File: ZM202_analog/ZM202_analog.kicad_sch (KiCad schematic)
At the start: 8 parts, among them U1 LM324, U13 LM393B

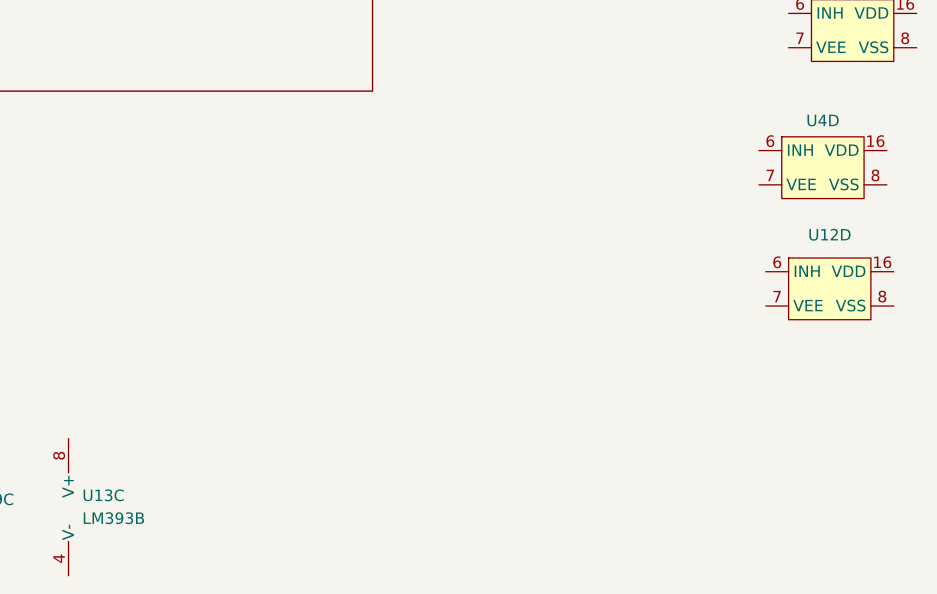
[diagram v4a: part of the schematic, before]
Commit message: Added PLL-circuit and added labels.
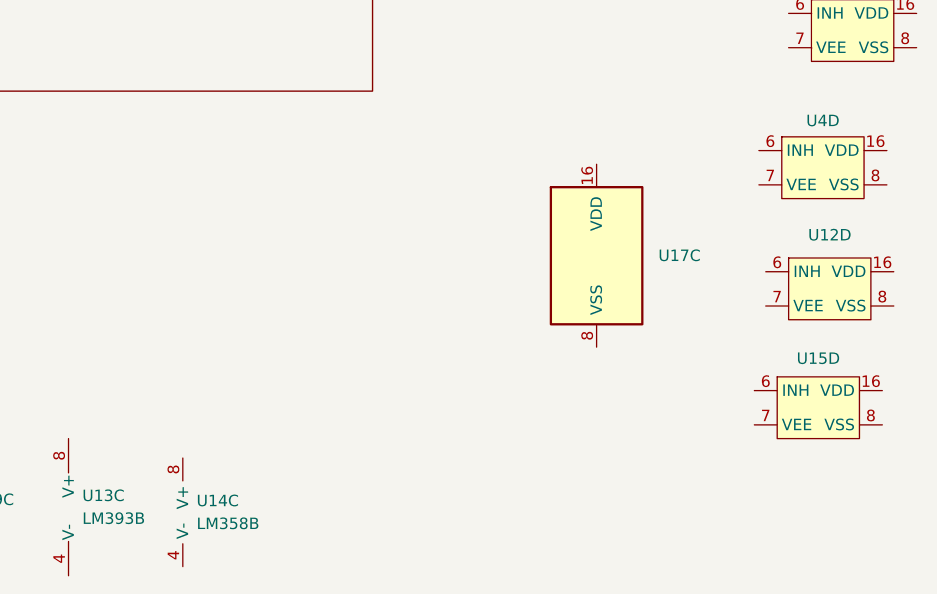
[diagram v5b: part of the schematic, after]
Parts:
- added U14: LM358B, Package_SO:SO-8_3.9x4.9mm_P1.27mm, symbol Jojos_Lib:LM358B
- added U15: ~, Package_SO:SOIC-16W_5.3x10.2mm_P1.27mm, symbol Jojos_Lib:CD4053
- added U17: ~, Package_SO:SO-16_3.9x9.9mm_P1.27mm, symbol Jojos_Lib:CD4027BM96
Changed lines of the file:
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@@
     (stroke (width 0) (type default))
+  )
+  (symbol (lib_id "Jojos_Lib:CD4027BM96") (at 175.514 137.16 0) (unit 3)
+    (in_bom yes) (on_board yes) (dnp no) (fields_autoplaced)
+    (property "Reference" "U17" (at 182.372 137.16 0)
+      (effects (font (size 1.27 1.27)) (justify left))
+    )
+    (property "Value" "~" (at 167.894 146.05 0)
+      (effects (font (size 1.27 1.27)))
+    )
+    (property "Footprint" "Package_SO:SO-16_3.9x9.9mm_P1.27mm" (at 175.514 137.16 0)
+      (effects (font (size 1.27 1.27)) hide)
+    )
+    (property "Datasheet" "http://www.intersil.com/content/dam/Intersil/documents/cd40/cd4027bms.pdf" (at 175.514 137.16 0)
+      (effects (font (size 1.27 1.27)) hide)
+    )
+    (property "Mouser Part Number" "595-CD4027BM96 " (at 175.514 137.16 0)
+      (effects (font (size 1.27 1.27)) hide)
+    )
+    (pin "1")
+    (pin "2")
+    (pin "3")
+    (pin "4")
+    (pin "5")
+    (pin "6")
+    (pin "7")
+    (pin "10")
+    (pin "11")
+    (pin "12")
+    (pin "13")
+    (pin "14")
+    (pin "15")
+    (pin "9")
+    (pin "16")
+    (pin "8")
+    (instances
+      (project "ZM202_analog"
+        (path "/99a04650-e6a5-4da0-b985-3216476cb3cd/42bdac79-14b2-41d3-9681-42fcfeb810b2"
+          (reference "U17") (unit 3)
+        )
+        (path "/99a04650-e6a5-4da0-b985-3216476cb3cd"
+          (reference "U17") (unit 3)
+        )
+      )
+    )
   )
   (symbol (lib_id "Jojos_Lib:LM324ADR ") (at 69.342 164.338 0) (unit 5)
@@
         (path "/99a04650-e6a5-4da0-b985-3216476cb3cd/623fe2f9-a117-4b04-94d6-8c06947e3053"
           (reference "U4") (unit 5)
+        )
+      )
+    )
+  )
+  (symbol (lib_id "Jojos_Lib:LM358B") (at 129.54 165.608 0) (unit 3)
+    (in_bom yes) (on_board yes) (dnp no) (fields_autoplaced)
+    (property "Reference" "U14" (at 131.064 164.4015 0)
+      (effects (font (size 1.27 1.27)) (justify left))
+    )
+    (property "Value" "LM358B" (at 131.064 166.9415 0)
+      (effects (font (size 1.27 1.27)) (justify left))
+    )
+    (property "Footprint" "Package_SO:SO-8_3.9x4.9mm_P1.27mm" (at 129.54 165.608 0)
+      (effects (font (size 1.27 1.27)) hide)
+    )
+    (property "Datasheet" "" (at 129.54 165.608 0)
+      (effects (font (size 1.27 1.27)) hide)
+    )
+    (property "Mouser Part Number" "595-LM358BAIDR " (at 129.54 165.608 0)
+      (effects (font (size 1.27 1.27)) hide)
+    )
+    (pin "1")
+    (pin "2")
+    (pin "3")
+    (pin "5")
+    (pin "6")
+    (pin "7")
+    (pin "4")
+    (pin "8")
+    (instances
+      (project "ZM202_analog"
+        (path "/99a04650-e6a5-4da0-b985-3216476cb3cd/42bdac79-14b2-41d3-9681-42fcfeb810b2"
+          (reference "U14") (unit 3)
+        )
+        (path "/99a04650-e6a5-4da0-b985-3216476cb3cd"
+          (reference "U14") (unit 3)
         )
       )
@@
         )
       )
+    )
+  )
+  (symbol (lib_id "Jojos_Lib:CD4053") (at 200.152 153.67 0) (unit 4)
+    (in_bom yes) (on_board yes) (dnp no) (fields_autoplaced)
+    (property "Reference" "U15" (at 200.152 148.59 0)
+      (effects (font (size 1.27 1.27)))
+    )
+    (property "Value" "~" (at 198.628 153.924 0)
+      (effects (font (size 1.27 1.27)))
+    )
+    (property "Footprint" "Package_SO:SOIC-16W_5.3x10.2mm_P1.27mm" (at 198.628 153.924 0)
+      (effects (font (size 1.27 1.27)) hide)
+    )
+    (property "Datasheet" "" (at 198.628 153.924 0)
+      (effects (font (size 1.27 1.27)) hide)
+    )
+    (property "Mouser Part Number" "595-CD4053BM96G3" (at 200.152 153.67 0)
+      (effects (font (size 1.27 1.27)) hide)
+    )
+    (pin "11")
+    (pin "12")
+    (pin "13")
+    (pin "14")
+    (pin "1")
+    (pin "10")
+    (pin "15")
+    (pin "2")
+    (pin "3")
+    (pin "4")
+    (pin "5")
+    (pin "9")
+    (pin "16")
+    (pin "6")
+    (pin "7")
+    (pin "8")
+    (instances
+      (project "ZM202_analog"
+        (path "/99a04650-e6a5-4da0-b985-3216476cb3cd/42bdac79-14b2-41d3-9681-42fcfeb810b2"
+          (reference "U15") (unit 4)
+        )
+        (path "/99a04650-e6a5-4da0-b985-3216476cb3cd"
+          (reference "U15") (unit 4)
+        )
+      )

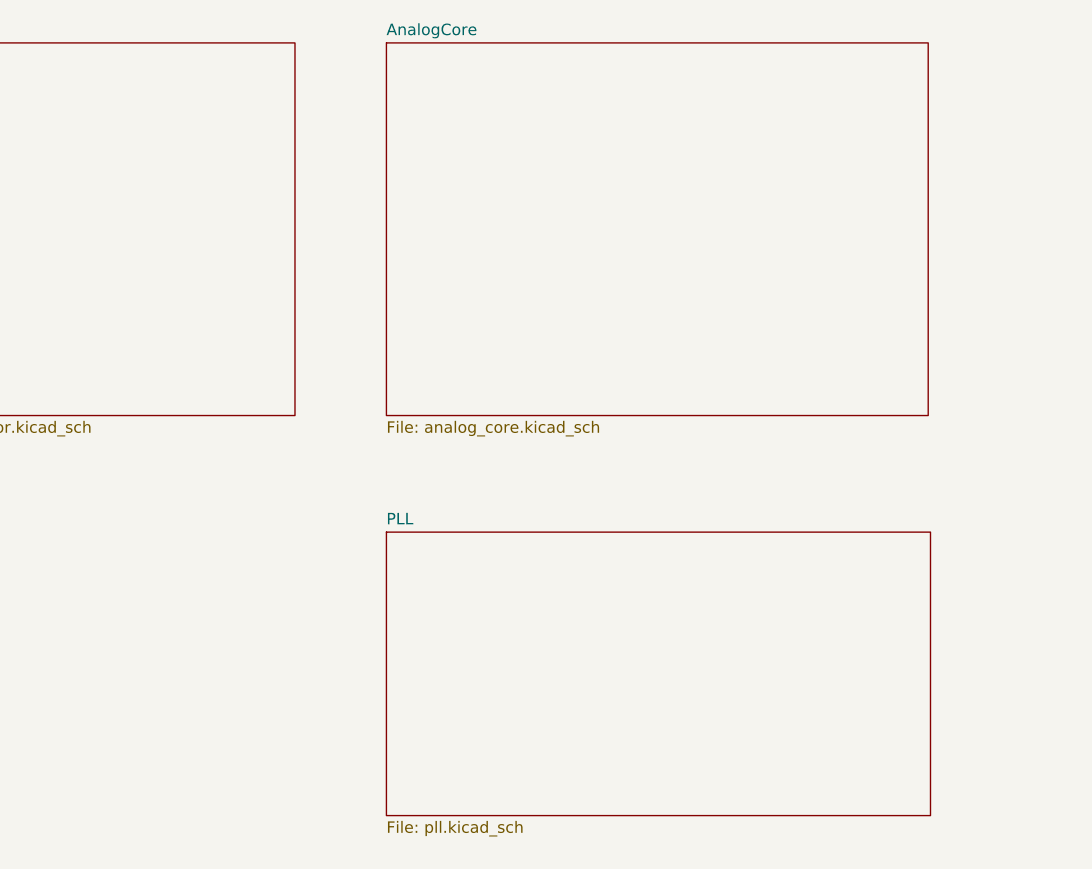
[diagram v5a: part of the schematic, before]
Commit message: Added labels and connections to outside-world.
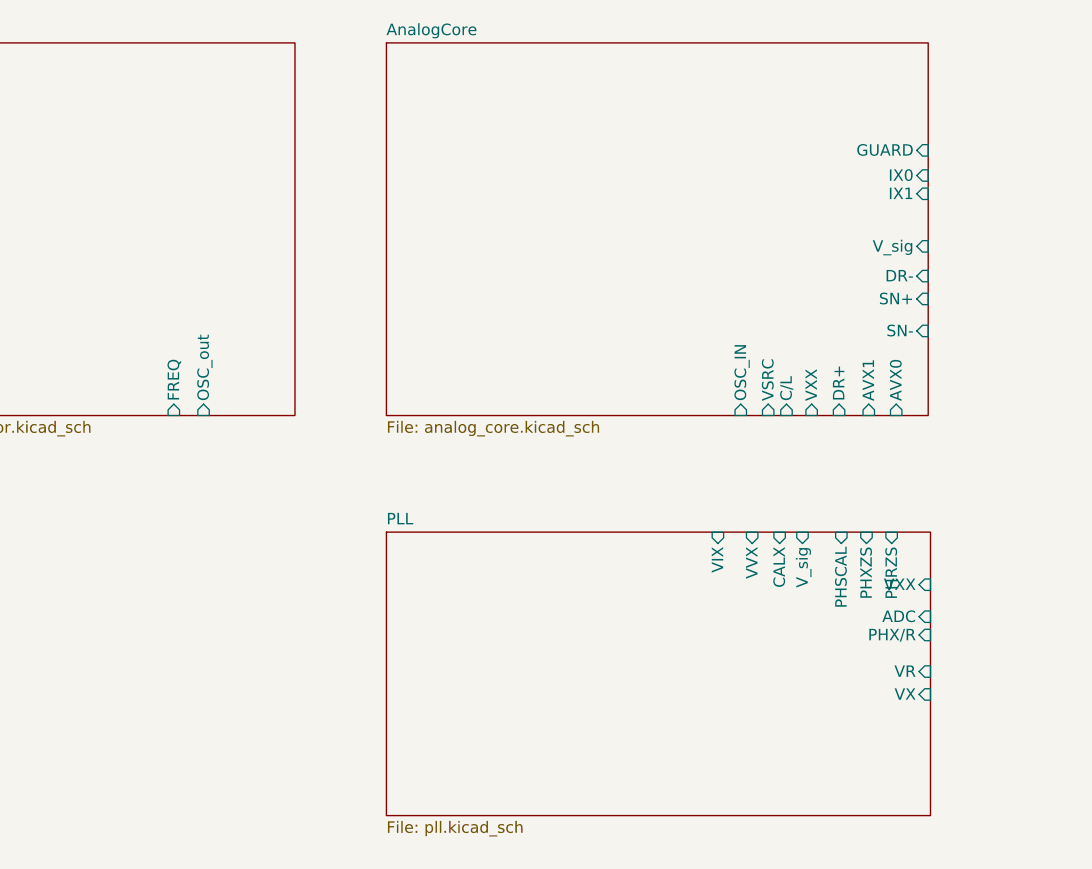
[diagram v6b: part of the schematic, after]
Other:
- sheet AnalogCore ports: added AVX0, AVX1, C/L, DR+, DR-, GUARD, IX0, IX1, OSC_IN, SN+, SN-, VSRC, VXX, V_sig; removed none
- sheet Oscillator ports: added FREQ, OSC_out; removed none
- sheet PLL ports: added ADC, CALX, PHRZS, PHSCAL, PHXZS, PHX/R, VIX, VR, VVX, VX, VXX, V_sig; removed none
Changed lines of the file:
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@@
       (effects (font (size 1.27 1.27)) (justify left top))
+    )
+    (pin "VX" input (at 150.622 105.41 0)
+      (effects (font (size 1.27 1.27)) (justify right))
+    )
+    (pin "VR" input (at 150.622 102.87 0)
+      (effects (font (size 1.27 1.27)) (justify right))
+    )
+    (pin "PHX{slash}R" input (at 150.622 98.806 0)
+      (effects (font (size 1.27 1.27)) (justify right))
+    )
+    (pin "ADC" input (at 150.622 96.774 0)
+      (effects (font (size 1.27 1.27)) (justify right))
+    )
+    (pin "VXX" input (at 150.622 93.218 0)
+      (effects (font (size 1.27 1.27)) (justify right))
+    )
+    (pin "PHRZS" input (at 146.304 87.376 90)
+      (effects (font (size 1.27 1.27)) (justify right))
+    )
+    (pin "PHXZS" input (at 143.51 87.376 90)
+      (effects (font (size 1.27 1.27)) (justify right))
+    )
+    (pin "PHSCAL" input (at 140.716 87.376 90)
+      (effects (font (size 1.27 1.27)) (justify right))
+    )
+    (pin "V_sig" input (at 136.398 87.376 90)
+      (effects (font (size 1.27 1.27)) (justify right))
+    )
+    (pin "CALX" input (at 133.858 87.376 90)
+      (effects (font (size 1.27 1.27)) (justify right))
+    )
+    (pin "VVX" input (at 130.81 87.376 90)
+      (effects (font (size 1.27 1.27)) (justify right))
+    )
+    (pin "VIX" input (at 127 87.376 90)
+      (effects (font (size 1.27 1.27)) (justify right))
     )
     (instances
@@
       (effects (font (size 1.27 1.27)) (justify left top))
     )
+    (pin "FREQ" input (at 66.548 74.422 270)
+      (effects (font (size 1.27 1.27)) (justify left))
+    )
+    (pin "OSC_out" input (at 69.85 74.422 270)
+      (effects (font (size 1.27 1.27)) (justify left))
+    )
     (instances
       (project "ZM202_analog"
@@
       (effects (font (size 1.27 1.27)) (justify left top))
     )
+    (pin "OSC_IN" input (at 129.54 74.422 270)
+      (effects (font (size 1.27 1.27)) (justify left))
+    )
+    (pin "VSRC" input (at 132.588 74.422 270)
+      (effects (font (size 1.27 1.27)) (justify left))
+    )
+    (pin "C{slash}L" input (at 134.62 74.422 270)
+      (effects (font (size 1.27 1.27)) (justify left))
+    )
+    (pin "VXX" input (at 137.414 74.422 270)
+      (effects (font (size 1.27 1.27)) (justify left))
+    )
+    (pin "DR+" input (at 140.462 74.422 270)
+      (effects (font (size 1.27 1.27)) (justify left))
+    )
+    (pin "AVX1" input (at 143.764 74.422 270)
+      (effects (font (size 1.27 1.27)) (justify left))
+    )
+    (pin "AVX0" input (at 146.812 74.422 270)
+      (effects (font (size 1.27 1.27)) (justify left))
+    )
+    (pin "SN-" input (at 150.368 65.024 0)
+      (effects (font (size 1.27 1.27)) (justify right))
+    )
+    (pin "SN+" input (at 150.368 61.468 0)
+      (effects (font (size 1.27 1.27)) (justify right))
+    )
+    (pin "DR-" input (at 150.368 58.928 0)
+      (effects (font (size 1.27 1.27)) (justify right))
+    )
+    (pin "V_sig" input (at 150.368 55.626 0)
+      (effects (font (size 1.27 1.27)) (justify right))
+    )
+    (pin "IX1" input (at 150.368 49.784 0)
+      (effects (font (size 1.27 1.27)) (justify right))
+    )
+    (pin "IX0" input (at 150.368 47.752 0)
+      (effects (font (size 1.27 1.27)) (justify right))
+    )
+    (pin "GUARD" input (at 150.368 44.958 0)
+      (effects (font (size 1.27 1.27)) (justify right))
+    )
     (instances

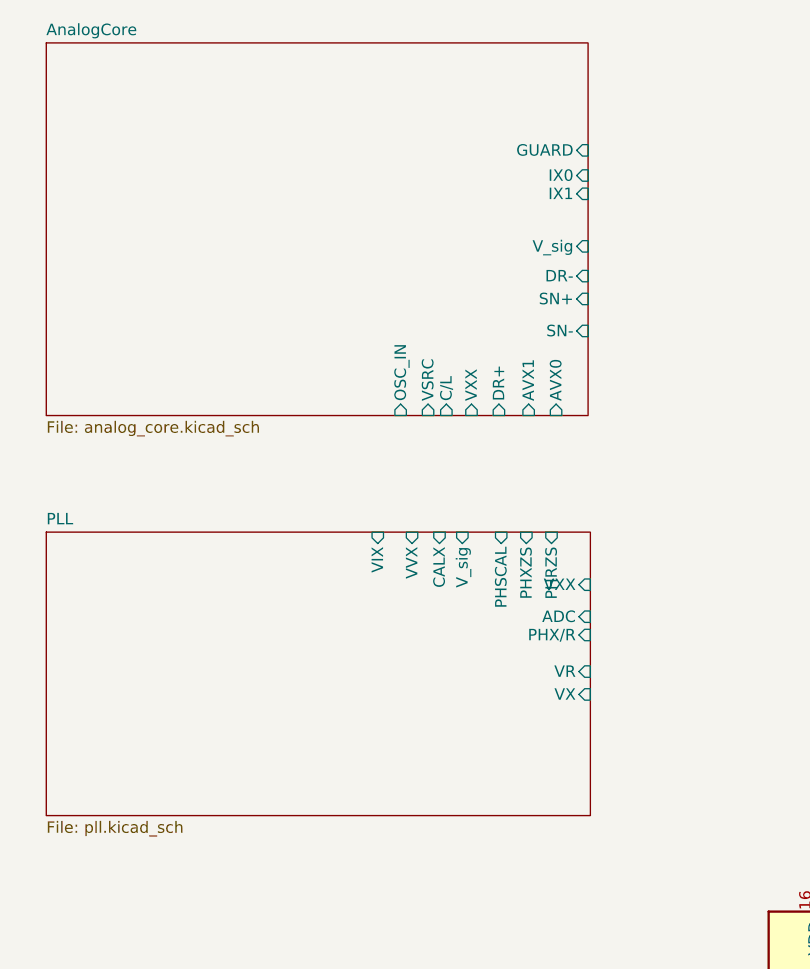
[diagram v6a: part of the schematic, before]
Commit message: Labels everywhere and connected hierarchical sheets.
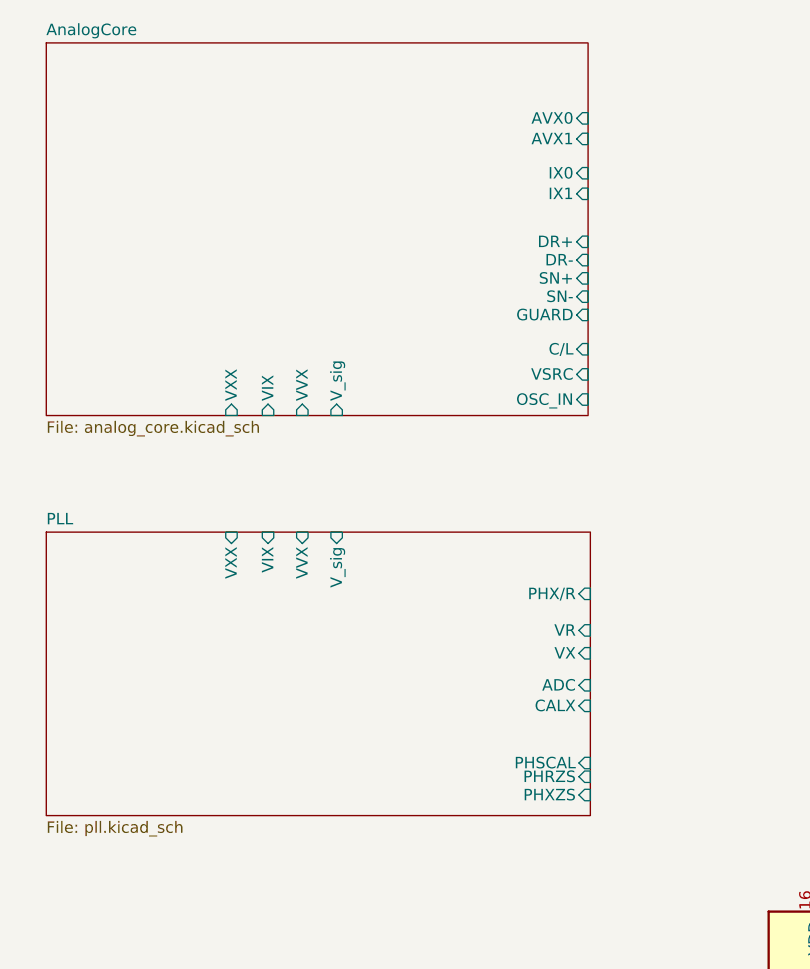
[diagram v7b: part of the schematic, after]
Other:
- sheet AnalogCore ports: added VIX, VVX; removed none
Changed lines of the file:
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@@
       (effects (font (size 1.27 1.27)) (justify left top))
     )
-    (pin "VX" input (at 150.622 105.41 0)
+    (pin "VX" input (at 150.622 100.838 0)
       (effects (font (size 1.27 1.27)) (justify right))
     )
-    (pin "VR" input (at 150.622 102.87 0)
+    (pin "VR" input (at 150.622 98.298 0)
       (effects (font (size 1.27 1.27)) (justify right))
     )
-    (pin "PHX{slash}R" input (at 150.622 98.806 0)
+    (pin "PHX{slash}R" input (at 150.622 94.234 0)
       (effects (font (size 1.27 1.27)) (justify right))
     )
-    (pin "ADC" input (at 150.622 96.774 0)
+    (pin "ADC" input (at 150.622 104.394 0)
       (effects (font (size 1.27 1.27)) (justify right))
     )
-    (pin "VXX" input (at 150.622 93.218 0)
+    (pin "VXX" input (at 110.744 87.376 90)
       (effects (font (size 1.27 1.27)) (justify right))
     )
-    (pin "PHRZS" input (at 146.304 87.376 90)
+    (pin "PHRZS" input (at 150.622 114.554 0)
       (effects (font (size 1.27 1.27)) (justify right))
     )
-    (pin "PHXZS" input (at 143.51 87.376 90)
+    (pin "PHXZS" input (at 150.622 116.586 0)
       (effects (font (size 1.27 1.27)) (justify right))
     )
-    (pin "PHSCAL" input (at 140.716 87.376 90)
+    (pin "PHSCAL" input (at 150.622 113.03 0)
       (effects (font (size 1.27 1.27)) (justify right))
     )
-    (pin "V_sig" input (at 136.398 87.376 90)
+    (pin "V_sig" input (at 122.428 87.376 90)
       (effects (font (size 1.27 1.27)) (justify right))
     )
-    (pin "CALX" input (at 133.858 87.376 90)
+    (pin "CALX" input (at 150.622 106.68 0)
       (effects (font (size 1.27 1.27)) (justify right))
     )
-    (pin "VVX" input (at 130.81 87.376 90)
+    (pin "VVX" input (at 118.618 87.376 90)
       (effects (font (size 1.27 1.27)) (justify right))
     )
-    (pin "VIX" input (at 127 87.376 90)
+    (pin "VIX" input (at 114.808 87.376 90)
       (effects (font (size 1.27 1.27)) (justify right))
     )
@@
       (effects (font (size 1.27 1.27)) (justify left top))
     )
-    (pin "OSC_IN" input (at 129.54 74.422 270)
+    (pin "OSC_IN" input (at 150.368 72.644 0)
+      (effects (font (size 1.27 1.27)) (justify right))
+    )
+    (pin "VSRC" input (at 150.368 69.85 0)
+      (effects (font (size 1.27 1.27)) (justify right))
+    )
+    (pin "C{slash}L" input (at 150.368 67.056 0)
+      (effects (font (size 1.27 1.27)) (justify right))
+    )
+    (pin "VXX" input (at 110.744 74.422 270)
       (effects (font (size 1.27 1.27)) (justify left))
     )
-    (pin "VSRC" input (at 132.588 74.422 270)
-      (effects (font (size 1.27 1.27)) (justify left))
-    )
-    (pin "C{slash}L" input (at 134.62 74.422 270)
-      (effects (font (size 1.27 1.27)) (justify left))
-    )
-    (pin "VXX" input (at 137.414 74.422 270)
-      (effects (font (size 1.27 1.27)) (justify left))
-    )
-    (pin "DR+" input (at 140.462 74.422 270)
-      (effects (font (size 1.27 1.27)) (justify left))
-    )
-    (pin "AVX1" input (at 143.764 74.422 270)
-      (effects (font (size 1.27 1.27)) (justify left))
-    )
-    (pin "AVX0" input (at 146.812 74.422 270)
-      (effects (font (size 1.27 1.27)) (justify left))
-    )
-    (pin "SN-" input (at 150.368 65.024 0)
+    (pin "DR+" input (at 150.368 55.118 0)
       (effects (font (size 1.27 1.27)) (justify right))
     )
-    (pin "SN+" input (at 150.368 61.468 0)
+    (pin "AVX1" input (at 150.368 43.688 0)
       (effects (font (size 1.27 1.27)) (justify right))
     )
-    (pin "DR-" input (at 150.368 58.928 0)
+    (pin "AVX0" input (at 150.368 41.402 0)
       (effects (font (size 1.27 1.27)) (justify right))
     )
-    (pin "V_sig" input (at 150.368 55.626 0)
+    (pin "SN-" input (at 150.368 61.214 0)
       (effects (font (size 1.27 1.27)) (justify right))
+    )
+    (pin "SN+" input (at 150.368 59.182 0)
+      (effects (font (size 1.27 1.27)) (justify right))
+    )
+    (pin "DR-" input (at 150.368 57.15 0)
+      (effects (font (size 1.27 1.27)) (justify right))
+    )
+    (pin "V_sig" input (at 122.428 74.422 270)
+      (effects (font (size 1.27 1.27)) (justify left))
     )
     (pin "IX1" input (at 150.368 49.784 0)
       (effects (font (size 1.27 1.27)) (justify right))
     )
-    (pin "IX0" input (at 150.368 47.752 0)
+    (pin "IX0" input (at 150.368 47.498 0)
       (effects (font (size 1.27 1.27)) (justify right))
     )
-    (pin "GUARD" input (at 150.368 44.958 0)
+    (pin "GUARD" input (at 150.368 63.246 0)
       (effects (font (size 1.27 1.27)) (justify right))
     )
+    (pin "VVX" input (at 118.618 74.422 270)
+      (effects (font (size 1.27 1.27)) (justify left))
+    )
+    (pin "VIX" input (at 114.808 74.422 270)
+      (effects (font (size 1.27 1.27)) (justify left))
+    )
     (instances
